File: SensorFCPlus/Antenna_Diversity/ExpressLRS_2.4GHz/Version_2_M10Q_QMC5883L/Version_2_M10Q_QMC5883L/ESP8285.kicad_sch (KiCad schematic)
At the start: 24 parts, among them U3 ESP8285H16, Y1 26MHz

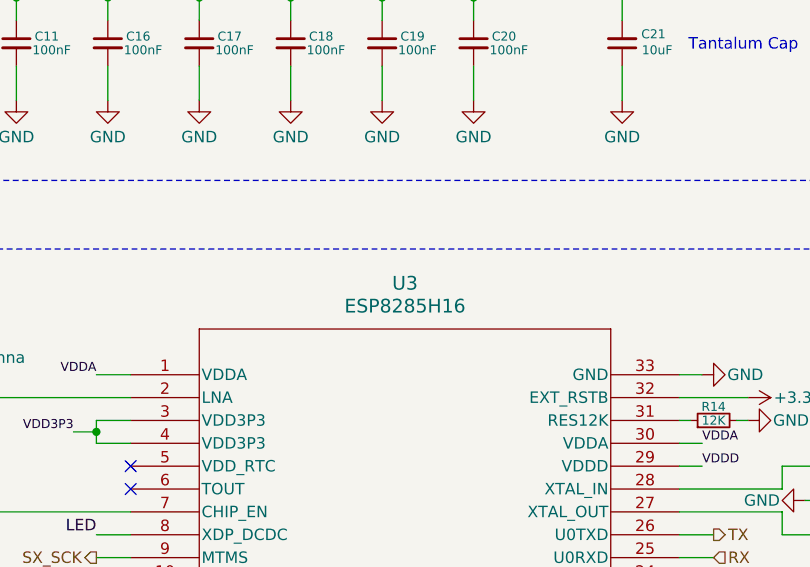
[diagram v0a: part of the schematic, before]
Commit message: Update README.md and Version 2 files; add new GIF and MP4 for Version 2
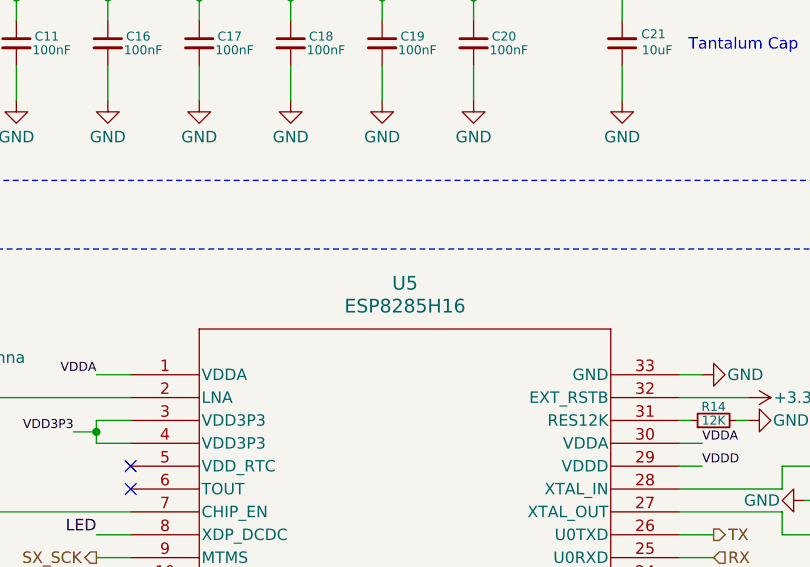
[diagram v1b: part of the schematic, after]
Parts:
- JP1: footprint TestPoint:TestPoint_2Pads_Pitch2.54mm_Drill0.8mm -> Jumper:SolderJumper-2_P1.3mm_Open_RoundedPad1.0x1.5mm
- renumbered U3 to U5
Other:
- company: (none) -> https://github.com/Paschalis
- title: (none) -> ESP8285
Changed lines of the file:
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@@
 	(generator_version "8.0")
 	(paper "A4")
+	(title_block
+		(title "ESP8285")
+		(date "2025-01-28")
+		(rev "1.0")
+		(company "https://github.com/Paschalis")
+		(comment 1 "based on signal strength.")
+		(comment 2 "SX1280 and manages antenna diversity by dynamically switching antennas ")
+		(comment 3 "Is used to flash the ELRS firmware for a 2.4GHz receiver. It controls the  ")
+	)
 	(junction
 		(at 152.4 46.99)
@@
 	(label "VDDA"
 		(at 177.8 96.52 0)
-		(fields_autoplaced yes)
 		(effects
 			(font
@@
 	(label "VDDD"
 		(at 78.74 46.99 180)
-		(fields_autoplaced yes)
 		(effects
 			(font
@@
 	(label "VDDA"
 		(at 110.49 88.9 180)
-		(fields_autoplaced yes)
 		(effects
 			(font
@@
 	(label "VDD3P3"
 		(at 107.95 95.25 180)
-		(fields_autoplaced yes)
 		(effects
 			(font
@@
 	(label "LED"
 		(at 110.49 106.68 180)
-		(fields_autoplaced yes)
 		(effects
 			(font
@@
 	(label "VDD3P3"
 		(at 78.74 39.37 180)
-		(fields_autoplaced yes)
 		(effects
 			(font
@@
 	(label "VDDD"
 		(at 177.8 99.06 0)
-		(fields_autoplaced yes)
 		(effects
 			(font
@@
 	(label "VDDPST"
 		(at 78.74 31.75 180)
-		(fields_autoplaced yes)
 		(effects
 			(font
@@
 	(label "VDDA"
 		(at 78.74 44.45 180)
-		(fields_autoplaced yes)
 		(effects
 			(font
@@
 	(label "VDDPST"
 		(at 78.74 34.29 180)
-		(fields_autoplaced yes)
 		(effects
 			(font
@@
 	(label "VDDA"
 		(at 78.74 41.91 180)
-		(fields_autoplaced yes)
 		(effects
 			(font
@@
 	(label "VDDPST"
 		(at 189.23 129.54 0)
-		(fields_autoplaced yes)
 		(effects
 			(font
@@
 	(label "LED"
 		(at 38.1 25.4 180)
-		(fields_autoplaced yes)
 		(effects
 			(font
@@
 	(label "VDDPST"
 		(at 100.33 114.3 180)
-		(fields_autoplaced yes)
 		(effects
 			(font
@@
 	(label "VDD3P3"
 		(at 78.74 36.83 180)
-		(fields_autoplaced yes)
 		(effects
 			(font
@@
 		(shape input)
 		(at 179.07 109.22 0)
-		(fields_autoplaced yes)
 		(effects
 			(font
@@
 		(shape input)
 		(at 179.07 111.76 0)
-		(fields_autoplaced yes)
 		(effects
 			(font
@@
 		(shape input)
 		(at 49.53 119.38 180)
-		(fields_autoplaced yes)
 		(effects
 			(font
@@
 		(shape output)
 		(at 110.49 109.22 180)
-		(fields_autoplaced yes)
 		(effects
 			(font
@@
 		(shape output)
 		(at 72.39 121.92 180)
-		(fields_autoplaced yes)
 		(effects
 			(font
@@
 		(shape output)
 		(at 177.8 127 0)
-		(fields_autoplaced yes)
 		(effects
 			(font
@@
 		(shape input)
 		(at 110.49 111.76 180)
-		(fields_autoplaced yes)
 		(effects
 			(font
@@
 		(shape output)
 		(at 177.8 124.46 0)
-		(fields_autoplaced yes)
 		(effects
 			(font
@@
 		(shape bidirectional)
 		(at 110.49 127 180)
-		(fields_autoplaced yes)
 		(effects
 			(font
@@
 		(shape output)
 		(at 179.07 106.68 0)
-		(fields_autoplaced yes)
 		(effects
 			(font
@@
 		(shape output)
 		(at 110.49 116.84 180)
-		(fields_autoplaced yes)
 		(effects
 			(font
@@
 			)
 		)
-		(property "Footprint" "TestPoint:TestPoint_2Pads_Pitch2.54mm_Drill0.8mm"
+		(property "Footprint" "Jumper:SolderJumper-2_P1.3mm_Open_RoundedPad1.0x1.5mm"
 			(at 99.06 137.16 0)
 			(effects
@@
 		(dnp no)
 		(fields_autoplaced yes)
-		(property "Reference" "U3"
+		(property "Reference" "U5"
 			(at 144.78 78.74 0)
 			(effects
@@
 			(project "Version_2_M10Q_QMC5883L"
 				(path "/9b601b2a-e8dd-477b-913e-01a336e391b8/0eece480-063f-4580-b091-876854fe6ebe"
-					(reference "U3")
+					(reference "U5")
 					(unit 1)
 				)
